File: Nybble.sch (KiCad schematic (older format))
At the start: 106 parts, among them J1 USB_mini_micro_B, SW1 SW_PUSH, U1 ATMEGA32U4, X1 XTAL_GND

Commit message: Fixed issues with the schematic
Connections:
- wire segments 162 -> 161
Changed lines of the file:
@@
 Wire Wire Line
 	7450 1450 8150 1450
-Connection ~ 4420 4265
-Connection ~ 4970 4265
-Connection ~ 5520 4265
-Connection ~ 6070 4265
-Connection ~ 6670 4265
 Wire Wire Line
 	1070 4965 7270 4965
@@
 	1620 6040 1620 6065
 Wire Wire Line
-	2290 6040 2170 6040
-Wire Wire Line
 	2170 6040 2170 6065
 Wire Wire Line
-	3440 6040 3320 6040
-Wire Wire Line
 	3320 6040 3320 6065
 Wire Wire Line
@@
 	7270 6040 7270 6065
 Wire Wire Line
-	1395 3790 1395 5835
+	1395 3790 1395 5840
 Connection ~ 1395 4540
 Wire Wire Line
 	1395 5190 1395 5185
 Connection ~ 1395 5185
-Wire Wire Line
-	1945 3840 1945 5845
-Connection ~ 1945 5190
-Connection ~ 1945 4540
 Wire Wire Line
 	2495 3840 2495 4540
@@
 Connection ~ 7595 5185
 Wire Wire Line
-	1070 4260 1070 4265
+	2170 5390 2295 5390
+Wire Wire Line
+	2170 6040 2295 6040
+Wire Wire Line
+	3320 6040 3445 6040
+Wire Wire Line
+	1945 3840 1945 5840
+Connection ~ 1945 4540
+Connection ~ 1945 5190
 Wire Wire Line
 	1070 4265 7270 4265
@@
 Connection ~ 2170 4265
 Connection ~ 2720 4265
+Connection ~ 3320 4265
 Connection ~ 3870 4265
-Connection ~ 3320 4265
-Wire Wire Line
-	2170 5390 2295 5390
+Connection ~ 4420 4265
+Connection ~ 4970 4265
+Connection ~ 5520 4265
+Connection ~ 6070 4265
+Connection ~ 6670 4265
 $EndSCHEMATC

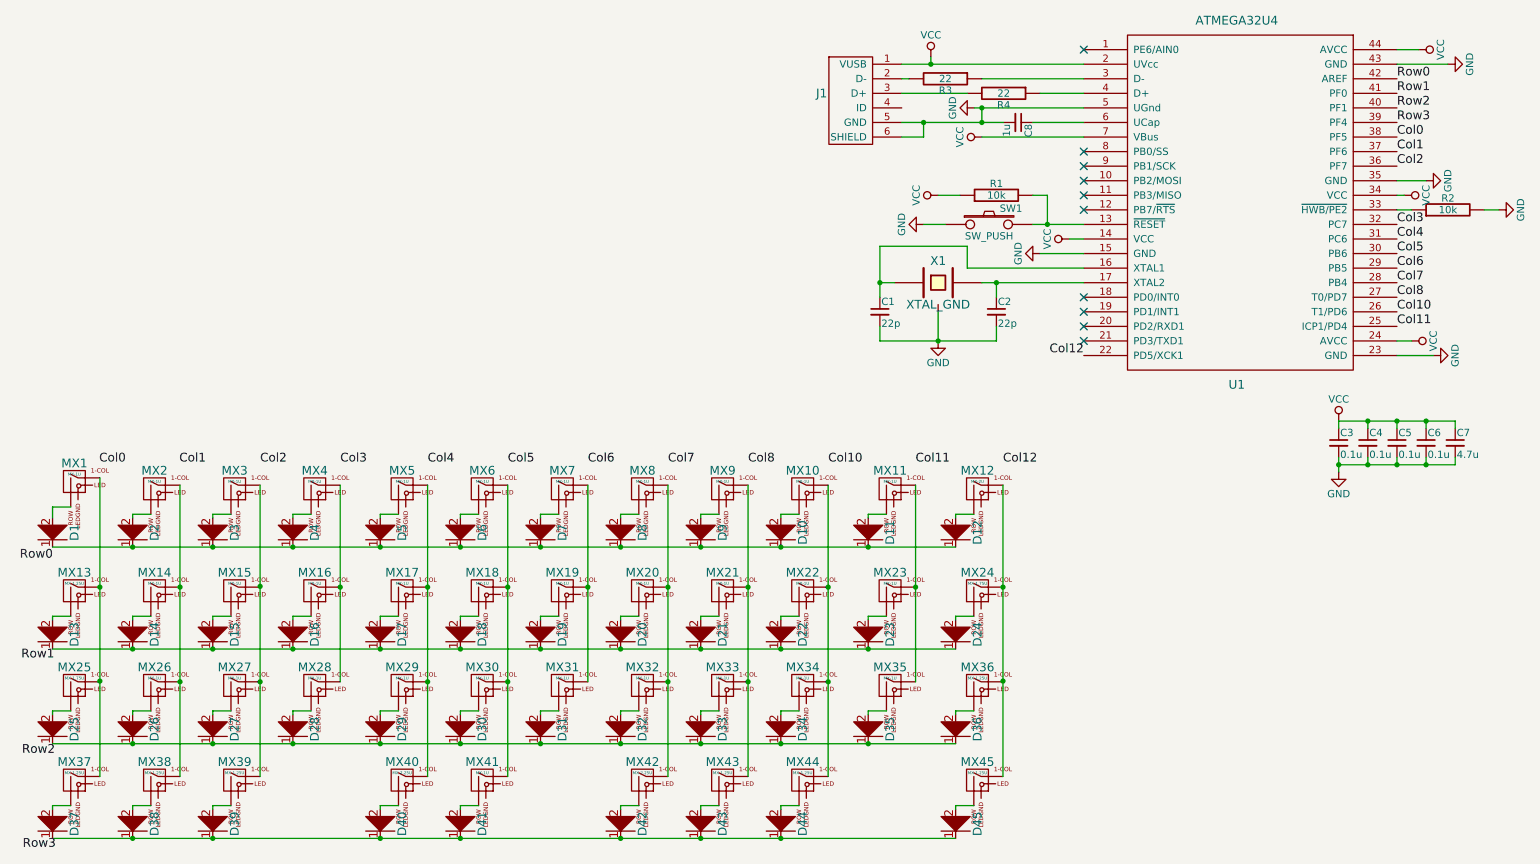
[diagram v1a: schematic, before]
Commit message: Fixed issues with the netlist
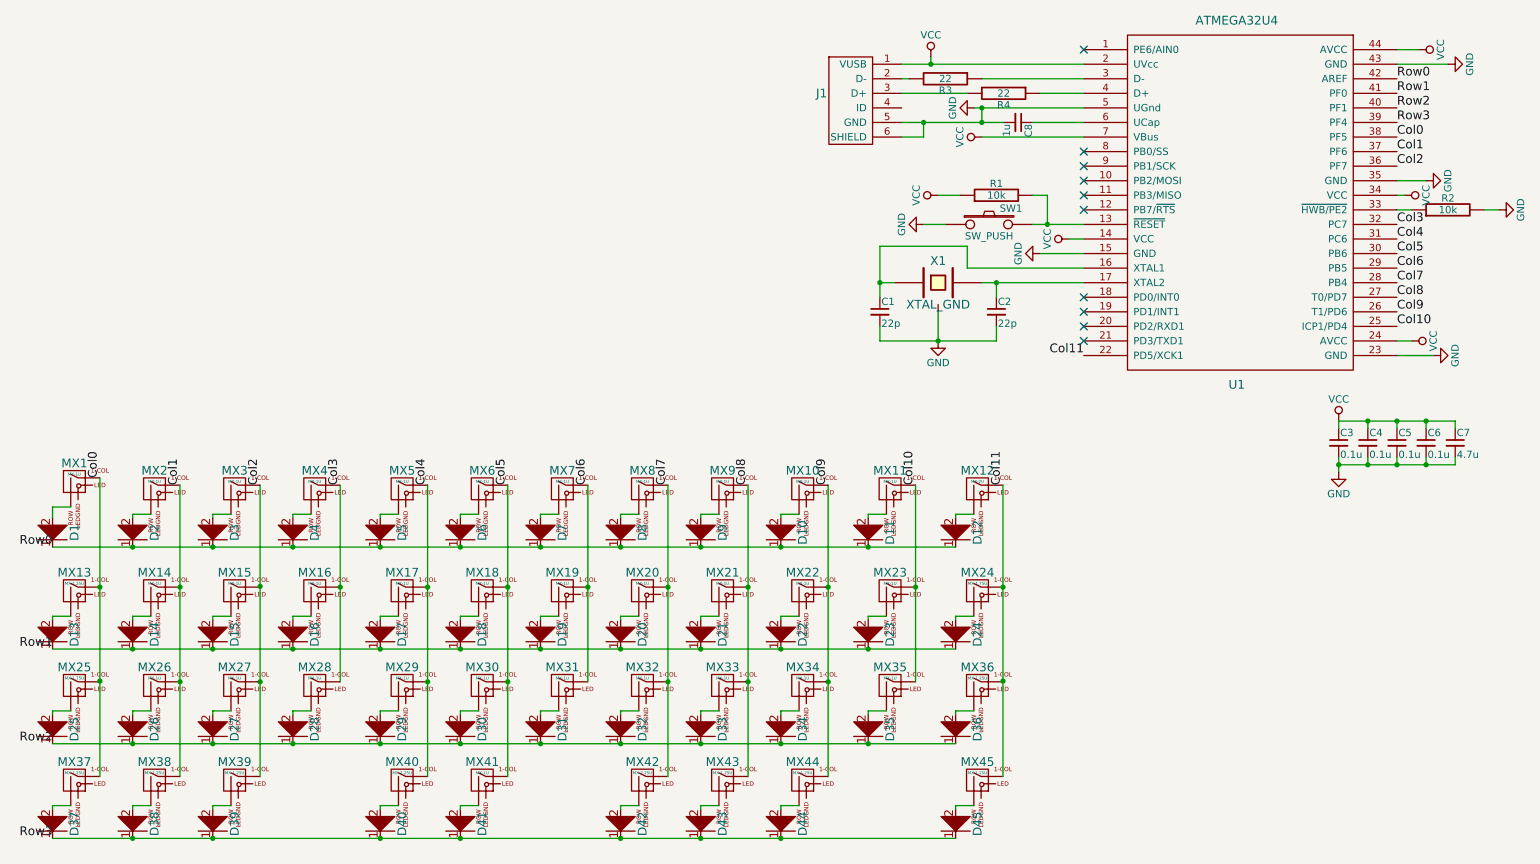
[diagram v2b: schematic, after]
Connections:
- net Col12 is gone; now on net Col11: U1.22 (PD5/XCK1)
- net Col0: now also MX1.1 (COL), MX13.1 (COL), MX25.1 (COL), MX37.1 (COL)
- net Col1: now also MX14.1 (COL), MX2.1 (COL), MX26.1 (COL), MX38.1 (COL)
- net Col10: now also MX11.1 (COL), MX23.1 (COL), MX35.1 (COL), U1.25 (ICP1/PD4); no longer U1.26 (T1/PD6)
- net Col11: now also MX12.1 (COL), MX24.1 (COL), MX36.1 (COL), MX45.1 (COL); no longer U1.25 (ICP1/PD4)
- net Col2: now also MX15.1 (COL), MX27.1 (COL), MX3.1 (COL), MX39.1 (COL)
- net Col3: now also MX16.1 (COL), MX28.1 (COL), MX4.1 (COL)
- net Col4: now also MX17.1 (COL), MX29.1 (COL), MX40.1 (COL), MX5.1 (COL)
- net Col5: now also MX18.1 (COL), MX30.1 (COL), MX41.1 (COL), MX6.1 (COL)
- net Col6: now also MX19.1 (COL), MX31.1 (COL), MX7.1 (COL)
- net Col7: now also MX20.1 (COL), MX32.1 (COL), MX42.1 (COL), MX8.1 (COL)
- net Col8: now also MX21.1 (COL), MX33.1 (COL), MX43.1 (COL), MX9.1 (COL)
- net Row0: now also D1.1, D10.1, D11.1, D12.1, D2.1, D3.1, D4.1, D5.1, D6.1, D7.1, D8.1, D9.1
- net Row1: now also D13.1, D14.1, D15.1, D16.1, D17.1, D18.1, D19.1, D20.1, D21.1, D22.1, D23.1, D24.1
- net Row2: now also D25.1, D26.1, D27.1, D28.1, D29.1, D30.1, D31.1, D32.1, D33.1, D34.1, D35.1, D36.1
- net Row3: now also D37.1, D38.1, D39.1, D40.1, D41.1, D42.1, D43.1, D44.1, D45.1
- net Col9: now reaches MX10.1 (COL), MX22.1 (COL), MX34.1 (COL), MX44.1 (COL)
- net Col9: now also U1.26 (T1/PD6)
